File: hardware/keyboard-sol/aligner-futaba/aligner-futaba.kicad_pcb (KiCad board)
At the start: 2 copper layers, 428.6 x 117.7 mm, 96 parts, among them SW10 TAB: 1.25x, SW11 I, SW12 2, SW13 Zero, SW14 Q, SW15 O, SW16 3, SW17 Dash, SW18 W, SW19 P, SW20 4, SW21 Caret, SW22 E, SW23 AT, SW24 5, SW25 LT Bracket, SW26 R, SW27 Return: 1.5x, SW28 6, SW29 Backslash, SW30 T, SW31 Line Feed, SW32 7, SW33 RT Bracket, SW34 Y, SW35 Load, SW36 LT Ctrl, SW37 J, SW38 Upper Case: 1.5x, SW39 M, SW4 ESC: 1.75x, SW40 Shift Lock: 1.5x, SW41 K, SW42 LT Shift: 1.5x, SW43 Comma, SW44 A, SW45 L, SW46 Z, SW47 Period, SW48 S, SW49 Semicolon, SW5 8, SW50 X, SW51 Slash, SW52 D, SW53 Colon, SW54 C, SW55 RT Shift: 2x, SW56 F, SW57 DEL, SW58 V, SW59 Mode Select: 1.75x, SW6 BREAK, SW60 G, SW61 Repeat: 1.25x, SW62 B, SW63 H, SW64 RT Ctrl, SW65 N, SW66 Local, SW67 NP Dash, SW68 NP 4, SW69 NP Zero, SW7 U, SW70 Up Arrow, SW71 NP 7, SW72 NP 1, SW73 NP period, SW74 LT Arrow, SW75 NP asterisk, SW76 NP 5, SW77 NP plus, SW78 Spacebar, SW79 NP 8, SW8 1, SW80 NP 2, SW81 RT Arrow, SW82 NP divide, SW83 NP 6, SW84 Down Arrow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

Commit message: Hole size adjustment
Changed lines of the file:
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@@
     (mod_text_size 1 1)
     (mod_text_width 0.15)
-    (pad_size 1.5875 1.5875)
-    (pad_drill 1.5875)
+    (pad_size 1.6256 1.6256)
+    (pad_drill 1.6256)
     (pad_to_mask_clearance 0)
     (aux_axis_origin 61.4172 179.1081)
@@
       (effects (font (size 1 1) (thickness 0.15)))
     )
-    (fp_line (start -63.3476 -5.6896) (end -63.3476 -1.397) (layer Edge.Cuts) (width 0.12))
-    (fp_line (start -70.0024 -5.6896) (end -63.3476 -5.6896) (layer Edge.Cuts) (width 0.12))
-    (fp_line (start -70.0024 -2.286) (end -70.0024 -5.6896) (layer Edge.Cuts) (width 0.12))
-    (fp_line (start -70.866 -2.286) (end -70.0024 -2.286) (layer Edge.Cuts) (width 0.12))
-    (fp_line (start -70.866 0.508) (end -70.866 -2.286) (layer Edge.Cuts) (width 0.12))
-    (fp_line (start -70.0024 0.508) (end -70.866 0.508) (layer Edge.Cuts) (width 0.12))
-    (fp_line (start -70.0024 6.604) (end -70.0024 0.508) (layer Edge.Cuts) (width 0.12))
-    (fp_line (start -68.199 6.604) (end -70.0024 6.604) (layer Edge.Cuts) (width 0.12))
-    (fp_line (start -68.199 7.7724) (end -68.199 6.604) (layer Edge.Cuts) (width 0.12))
-    (fp_line (start -65.151 7.7724) (end -68.199 7.7724) (layer Edge.Cuts) (width 0.12))
-    (fp_line (start -65.151 6.604) (end -65.151 7.7724) (layer Edge.Cuts) (width 0.12))
-    (fp_line (start -63.3476 6.604) (end -65.151 6.604) (layer Edge.Cuts) (width 0.12))
-    (fp_line (start -63.3476 1.397) (end -63.3476 6.604) (layer Edge.Cuts) (width 0.12))
-    (fp_line (start 63.3476 6.604) (end 63.3476 1.397) (layer Edge.Cuts) (width 0.12))
-    (fp_line (start 65.151 6.604) (end 63.3476 6.604) (layer Edge.Cuts) (width 0.12))
-    (fp_line (start 65.151 7.7724) (end 65.151 6.604) (layer Edge.Cuts) (width 0.12))
-    (fp_line (start 68.199 7.7724) (end 65.151 7.7724) (layer Edge.Cuts) (width 0.12))
-    (fp_line (start 68.199 6.604) (end 68.199 7.7724) (layer Edge.Cuts) (width 0.12))
-    (fp_line (start 70.0024 6.604) (end 68.199 6.604) (layer Edge.Cuts) (width 0.12))
-    (fp_line (start 70.0024 0.508) (end 70.0024 6.604) (layer Edge.Cuts) (width 0.12))
-    (fp_line (start 70.866 0.508) (end 70.0024 0.508) (layer Edge.Cuts) (width 0.12))
-    (fp_line (start 70.866 -2.286) (end 70.866 0.508) (layer Edge.Cuts) (width 0.12))
-    (fp_line (start 70.0024 -2.286) (end 70.866 -2.286) (layer Edge.Cuts) (width 0.12))
-    (fp_line (start 70.0024 -5.6896) (end 70.0024 -2.286) (layer Edge.Cuts) (width 0.12))
-    (fp_line (start 63.3476 -5.6896) (end 70.0024 -5.6896) (layer Edge.Cuts) (width 0.12))
-    (fp_line (start 63.3476 -1.397) (end 63.3476 -5.6896) (layer Edge.Cuts) (width 0.12))
-    (fp_line (start 7.697216 1.397) (end 63.3476 1.397) (layer Edge.Cuts) (width 0.12))
-    (fp_line (start 7.697216 -1.397) (end 63.3476 -1.397) (layer Edge.Cuts) (width 0.12))
-    (fp_line (start -63.3476 -1.397) (end -7.697216 -1.397) (layer Edge.Cuts) (width 0.12))
-    (fp_line (start -63.3476 1.397) (end -7.697216 1.397) (layer Edge.Cuts) (width 0.12))
     (fp_text user MX_space_aligner (at -0.6096 7.9248) (layer B.Fab)
       (effects (font (size 1 1) (thickness 0.15)))
@@
     (fp_arc (start 0 0) (end 7.697216 -1.397) (angle -159.4) (layer Edge.Cuts) (width 0.12))
     (fp_arc (start 0 0) (end -7.697216 1.397) (angle -159.4) (layer Edge.Cuts) (width 0.12))
+    (fp_line (start -63.2206 -5.6896) (end -63.2206 -1.397) (layer Edge.Cuts) (width 0.12))
+    (fp_line (start -70.1294 -5.6896) (end -63.2206 -5.6896) (layer Edge.Cuts) (width 0.12))
+    (fp_line (start -70.1294 -2.286) (end -70.1294 -5.6896) (layer Edge.Cuts) (width 0.12))
+    (fp_line (start -70.866 -2.286) (end -70.1294 -2.286) (layer Edge.Cuts) (width 0.12))
+    (fp_line (start -70.866 0.508) (end -70.866 -2.286) (layer Edge.Cuts) (width 0.12))
+    (fp_line (start -70.1294 0.508) (end -70.866 0.508) (layer Edge.Cuts) (width 0.12))
+    (fp_line (start -70.1294 6.604) (end -70.1294 0.508) (layer Edge.Cuts) (width 0.12))
+    (fp_line (start -68.199 6.604) (end -70.1294 6.604) (layer Edge.Cuts) (width 0.12))
+    (fp_line (start -68.199 7.7724) (end -68.199 6.604) (layer Edge.Cuts) (width 0.12))
+    (fp_line (start -65.151 7.7724) (end -68.199 7.7724) (layer Edge.Cuts) (width 0.12))
+    (fp_line (start -65.151 6.604) (end -65.151 7.7724) (layer Edge.Cuts) (width 0.12))
+    (fp_line (start -63.2206 6.604) (end -65.151 6.604) (layer Edge.Cuts) (width 0.12))
+    (fp_line (start -63.2206 1.397) (end -63.2206 6.604) (layer Edge.Cuts) (width 0.12))
+    (fp_line (start 63.2206 6.604) (end 63.2206 1.397) (layer Edge.Cuts) (width 0.12))
+    (fp_line (start 65.151 6.604) (end 63.2206 6.604) (layer Edge.Cuts) (width 0.12))
+    (fp_line (start 65.151 7.7724) (end 65.151 6.604) (layer Edge.Cuts) (width 0.12))
+    (fp_line (start 68.199 7.7724) (end 65.151 7.7724) (layer Edge.Cuts) (width 0.12))
+    (fp_line (start 68.199 6.604) (end 68.199 7.7724) (layer Edge.Cuts) (width 0.12))
+    (fp_line (start 70.1294 6.604) (end 68.199 6.604) (layer Edge.Cuts) (width 0.12))
+    (fp_line (start 70.1294 0.508) (end 70.1294 6.604) (layer Edge.Cuts) (width 0.12))
+    (fp_line (start 70.866 0.508) (end 70.1294 0.508) (layer Edge.Cuts) (width 0.12))
+    (fp_line (start 70.866 -2.286) (end 70.866 0.508) (layer Edge.Cuts) (width 0.12))
+    (fp_line (start 70.1294 -2.286) (end 70.866 -2.286) (layer Edge.Cuts) (width 0.12))
+    (fp_line (start 70.1294 -5.6896) (end 70.1294 -2.286) (layer Edge.Cuts) (width 0.12))
+    (fp_line (start 63.2206 -5.6896) (end 70.1294 -5.6896) (layer Edge.Cuts) (width 0.12))
+    (fp_line (start 63.2206 -1.397) (end 63.2206 -5.6896) (layer Edge.Cuts) (width 0.12))
+    (fp_line (start 7.697216 1.397) (end 63.2206 1.397) (layer Edge.Cuts) (width 0.12))
+    (fp_line (start 7.697216 -1.397) (end 63.2206 -1.397) (layer Edge.Cuts) (width 0.12))
+    (fp_line (start -63.2206 -1.397) (end -7.697216 -1.397) (layer Edge.Cuts) (width 0.12))
+    (fp_line (start -63.2206 1.397) (end -7.697216 1.397) (layer Edge.Cuts) (width 0.12))
     (pad "" np_thru_hole circle (at -6.985 6.985) (size 1.6256 1.6256) (drill 1.6256) (layers *.Cu *.Mask))
     (pad "" np_thru_hole circle (at -6.985 -6.985) (size 1.6256 1.6256) (drill 1.6256) (layers *.Cu *.Mask))
@@
       (effects (font (size 1 1) (thickness 0.15)))
     )
-    (pad "" np_thru_hole circle (at 0 0) (size 1.5875 1.5875) (drill 1.5875) (layers *.Cu *.Mask))
+    (pad "" np_thru_hole circle (at 0 0) (size 1.6256 1.6256) (drill 1.6256) (layers *.Cu *.Mask))
   )
   (module MountingHole:MountingHole_3.2mm_M3 (layer F.Cu)
@@
       (effects (font (size 1 1) (thickness 0.15)))
     )
-    (pad "" np_thru_hole circle (at 0 0) (size 1.5875 1.5875) (drill 1.5875) (layers *.Cu *.Mask))
+    (pad "" np_thru_hole circle (at 0 0) (size 1.6256 1.6256) (drill 1.6256) (layers *.Cu *.Mask))
   )
   (module unikbd:Futaba_2u_Cherry_aligner locked (layer F.Cu)

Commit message: tweaks for Cherry MX stabilizer posts on Futaba aligners
- Slightly narrower posts.
- slightly smaller hole, closer to end
- added mouse bites for breakaway to avoid protruding breakaway
- Applied to Sol and Classic
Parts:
- added REF**: Rod sizing hole 1/16 inch, MountingHole:MountingHole_3.2mm_M3, F.Cu at (87.0, 165.2)
- added REF**: Rod sizing hole 1/16 inch, MountingHole:MountingHole_3.2mm_M3, F.Cu at (495.2, 167.2)
- added REF**: Rod sizing hole 1/16 inch, MountingHole:MountingHole_3.2mm_M3, F.Cu at (495.2, 169.5)
- added REF**: Rod sizing hole 1/16 inch, MountingHole:MountingHole_3.2mm_M3, F.Cu at (495.2, 171.9)
- added REF**: Rod sizing hole 1/16 inch, MountingHole:MountingHole_3.2mm_M3, F.Cu at (87.0, 167.6)
- added REF**: Rod sizing hole 1/16 inch, MountingHole:MountingHole_3.2mm_M3, F.Cu at (87.0, 169.9)
- added REF**: Rod sizing hole 1/16 inch, MountingHole:MountingHole_3.2mm_M3, F.Cu at (289.0, 113.6)
- added REF**: Rod sizing hole 1/16 inch, MountingHole:MountingHole_3.2mm_M3, F.Cu at (291.3, 113.6)
- added REF**: Rod sizing hole 1/16 inch, MountingHole:MountingHole_3.2mm_M3, F.Cu at (293.7, 113.6)
- added REF**: Rod sizing hole 1/16 inch, MountingHole:MountingHole_3.2mm_M3, F.Cu at (368.4, 113.7)
- added REF**: Rod sizing hole 1/16 inch, MountingHole:MountingHole_3.2mm_M3, F.Cu at (370.7, 113.7)
- added REF**: Rod sizing hole 1/16 inch, MountingHole:MountingHole_3.2mm_M3, F.Cu at (373.1, 113.7)
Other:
- outline, holes or cut-outs redrawn

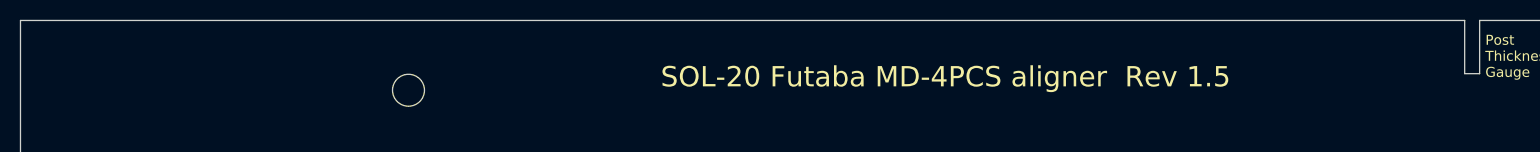
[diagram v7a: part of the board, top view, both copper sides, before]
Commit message: Fixed futaba posts on SOl-20 futaba aligner
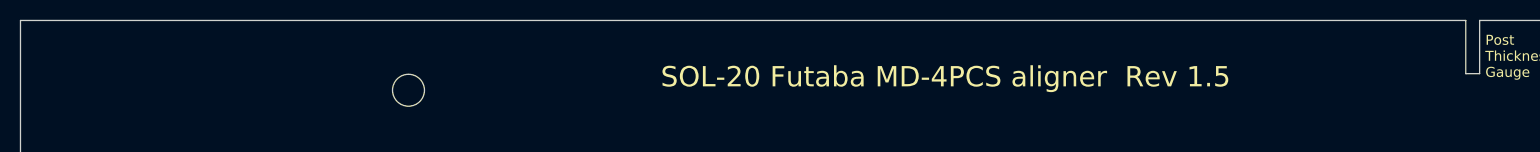
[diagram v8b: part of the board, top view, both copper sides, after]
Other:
- outline, holes or cut-outs redrawn
